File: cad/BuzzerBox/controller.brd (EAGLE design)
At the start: 100 x 100 mm, 131 parts, among them J2 RASPBERRYPI-40-PIN-GPIO_PTH_N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, Q1 BSS138, Q2 BSS138, Q3 BSS138, T1 BC849, T10 BC849, T2 BC849, T3 BC849, T4 BC849, T5 BC849, T6 BC849, T7 BC849, T8 BC849, T9 BC849, U1 ATMEGA328P-AU, Y1 16MHz

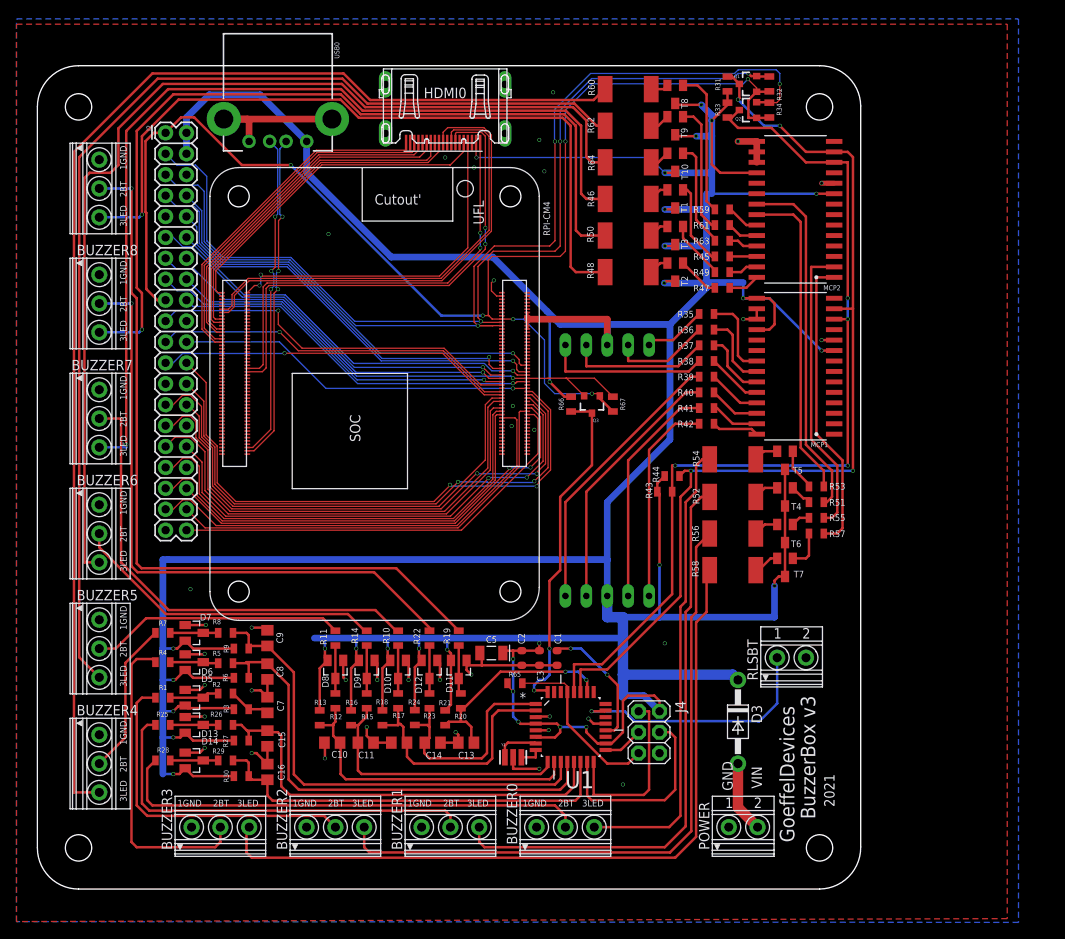
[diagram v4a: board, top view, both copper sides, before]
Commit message: Length match differential paris
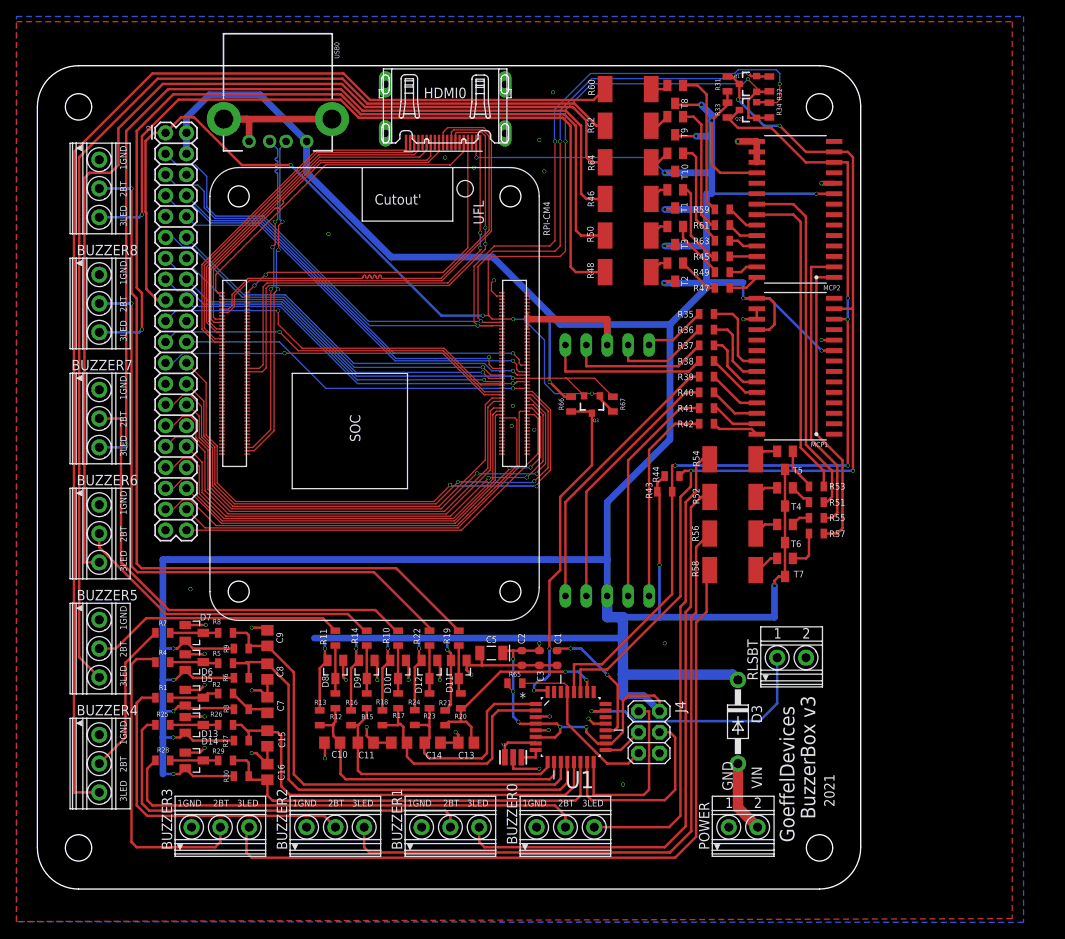
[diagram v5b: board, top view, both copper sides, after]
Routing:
- net SDAPI: track 115.7 -> 113.3 mm
- net SCLPI: track 124.0 -> 121.6 mm
- net GP4: track 52.5 -> 50.2 mm
- net GP14: track 52.5 -> 50.2 mm
- net HDMI_CLK_N: track 54.9 -> 56.6 mm
- net GP15: track 50.8 -> 49.6 mm
- net HDMI_SDA: track 42.7 -> 41.8 mm
- net USB_P: track 39.7 -> 40.4 mm

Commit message: Beef up power 5V power line
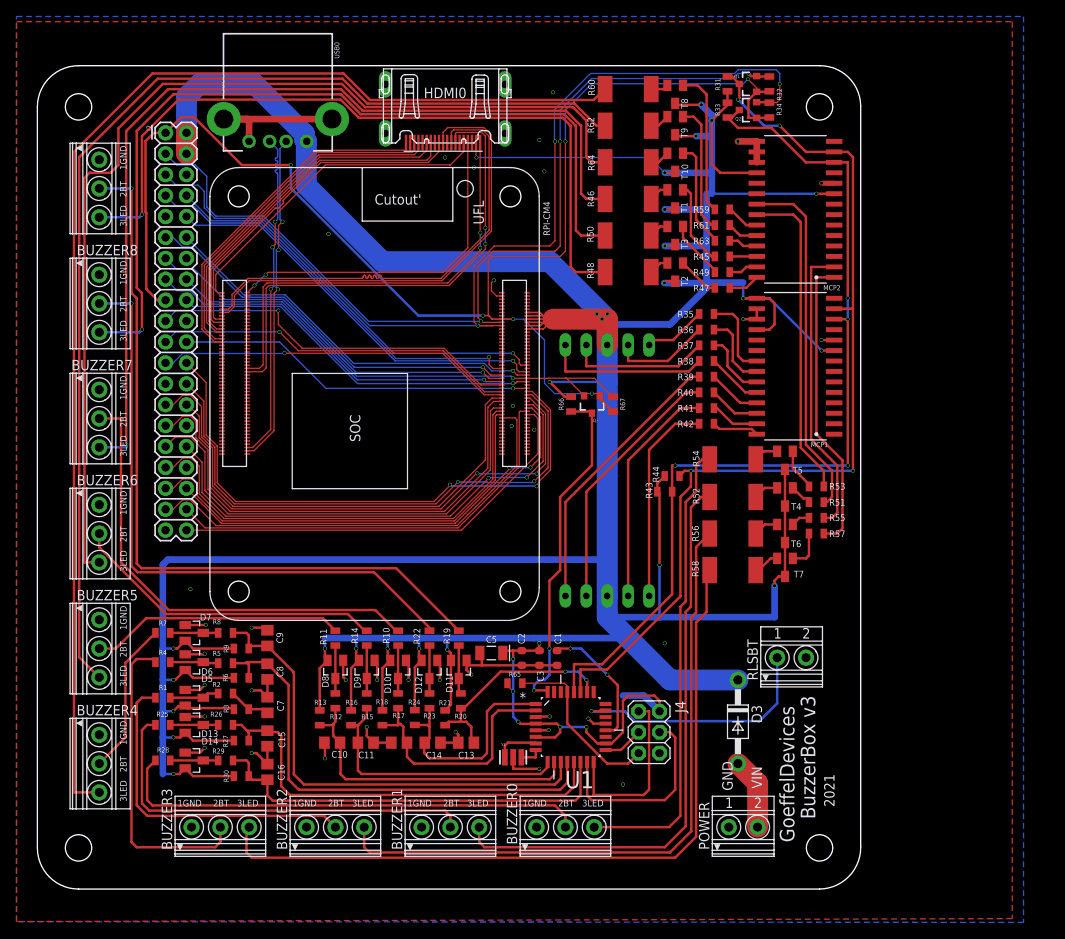
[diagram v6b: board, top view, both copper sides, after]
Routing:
- net +5V: track 636.9 -> 655.1 mm, vias 30 -> 33
- net +3V3: track 164.0 -> 165.7 mm

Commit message: Connect necessary CM4 pins, according to documentation
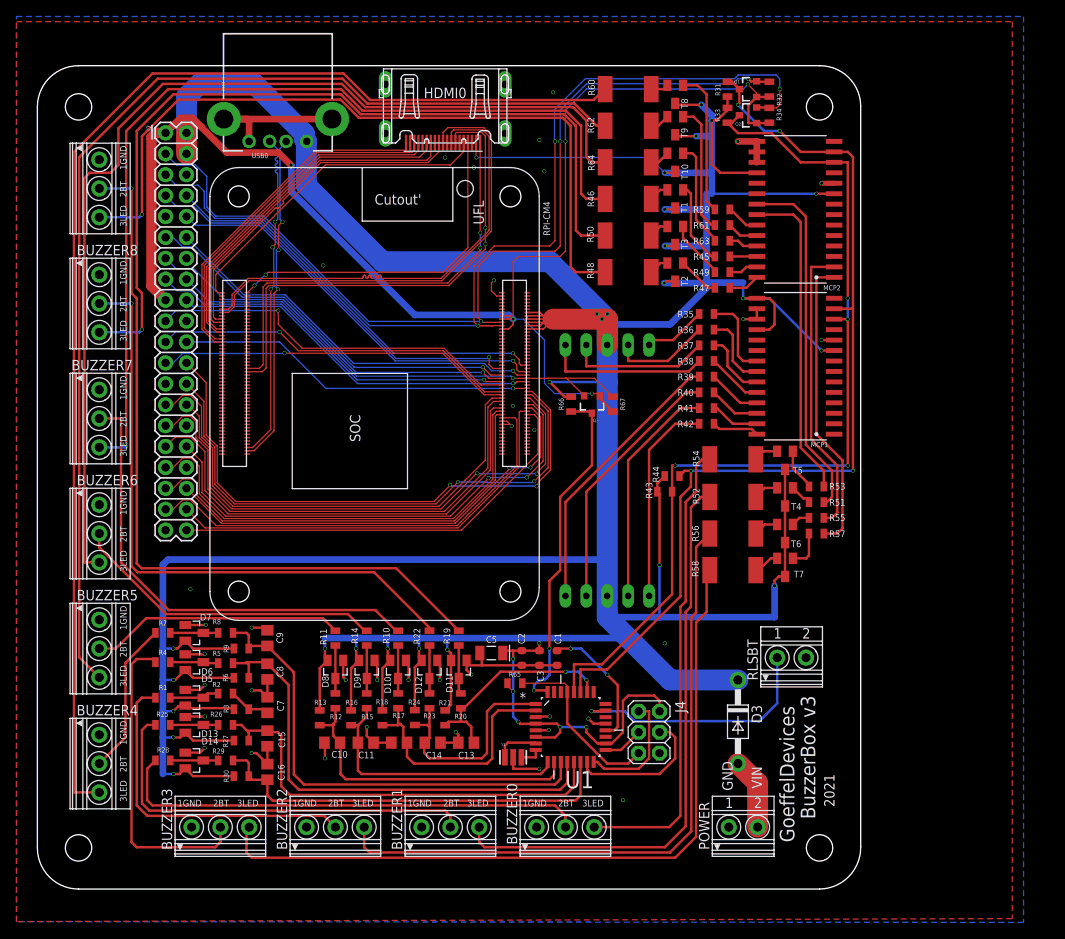
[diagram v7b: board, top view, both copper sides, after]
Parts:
- moved Q1 0.64 mm to (86.4, 97.2)
- moved R31 0.64 mm to (83.8, 97.2)
- moved R32 0.64 mm to (88.9, 97.2)
- moved Q2 0.63 mm to (86.4, 94.0)
- moved R33 0.63 mm to (83.8, 94.0)
- moved R34 0.63 mm to (88.9, 94.0)
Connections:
- net +3V3: now also RPI-CM4.78, RPI-CM4.86
- net GND: now also RPI-CM4.20
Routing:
- net +5V: track 655.1 -> 646.5 mm
- net MISO: track 21.8 -> 14.6 mm
- net MOSI: track 24.1 -> 17.4 mm
- net +3V3: track 165.7 -> 168.5 mm, vias 6 -> 5
- net GND: track 100.9 -> 103.6 mm

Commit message: Ground HDMI chassis, add overvoltage protection
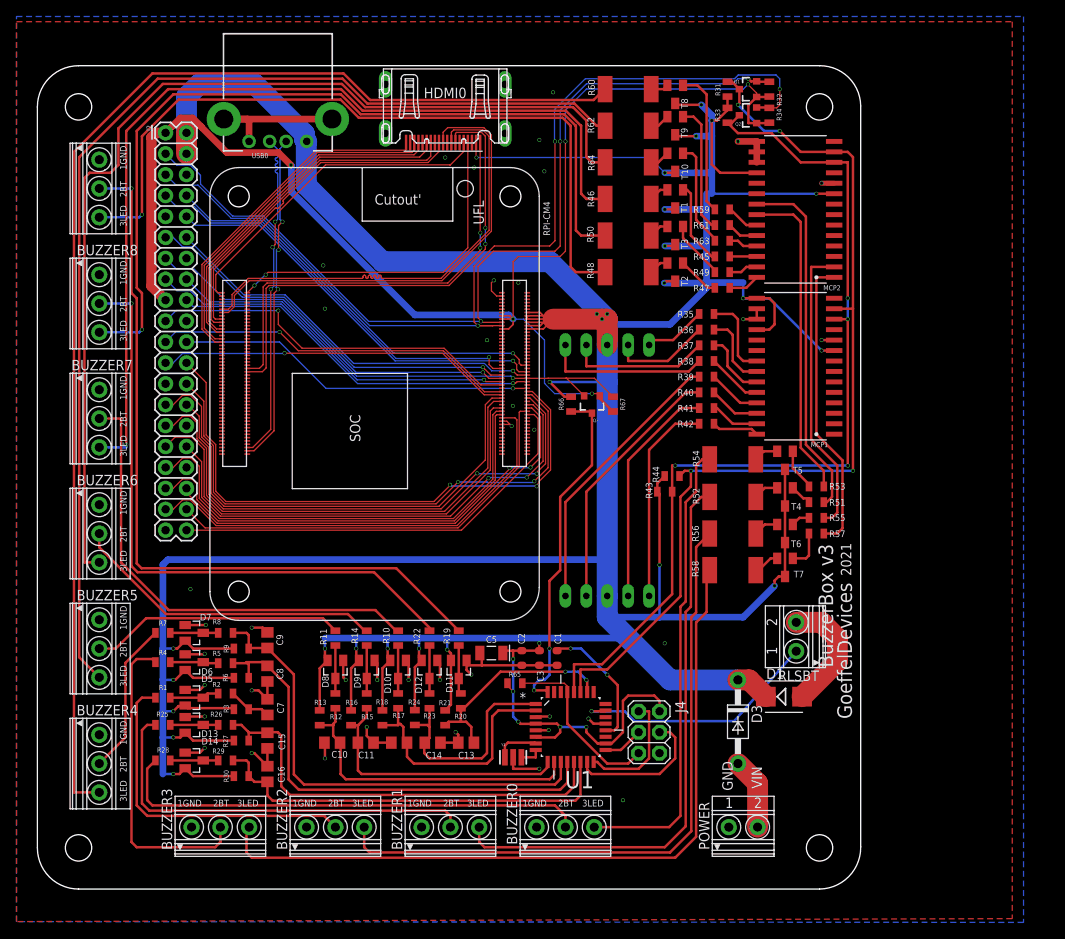
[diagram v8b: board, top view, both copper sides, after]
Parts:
- added D1: (no value), diode:SMB
- moved RLSBT 2.49 mm to (92.1, 30.6), turned to 90 degrees
- moved C15 0.25 mm to (27.9, 18.0)
- moved C7 0.25 mm to (27.9, 22.1)
- moved C8 0.25 mm to (27.9, 26.2)
- moved C9 0.25 mm to (27.9, 30.2)
- moved C16 0.25 mm to (27.9, 14.0)
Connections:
- net +5V: now also D1.C
- net GND: now also D1.A, HDMI0.P$24, HDMI0.P$25, HDMI0.P$26, HDMI0.P$27
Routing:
- net GND: track 103.6 -> 118.6 mm, vias 37 -> 40
- net +5V: track 646.5 -> 648.5 mm
- net SDAPI: track 113.0 -> 111.4 mm
- net SCLPI: track 121.4 -> 120.2 mm
- net GP8: track 70.6 -> 71.3 mm
- net GP7: track 67.2 -> 67.9 mm
- net ID_SD: track 61.1 -> 61.8 mm
- net ID_SC: track 64.6 -> 65.2 mm
- net GP6: track 57.5 -> 58.1 mm
- net GP5: track 59.9 -> 60.5 mm
